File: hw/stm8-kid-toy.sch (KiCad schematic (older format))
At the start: 13 parts, among them SW1 SW_Push, SW2 SW_Push, SW3 SW_Push, U1 STM8S003F3P

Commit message: hw: change multiplexing
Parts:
- removed D4, D5, D6: DIODE, symbol Simulation_SPICE:DIODE
- removed R1, R2, R3: R, symbol Device:R
- added D?: DIODE, symbol Simulation_SPICE:DIODE
- added R? (x6): R, symbol Device:R
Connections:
- net BTN1: now also SW1.2, R?.1
- net BTN2: now also SW2.2, R?.1
- net BTN3: now also SW3.2, R?.1
- net COM1: now also D1.2 (A), D2.2 (A), D3.2 (A), D?.1 (A); no longer SW1.1, SW2.1, SW3.1
- net GND: now also R?.2, R?.2, R?.2
- net LED1: now also R?.1; no longer D1.1 (K)
- net LED2: now also R?.1; no longer D2.1 (K)
- net LED3: now also R?.1; no longer D3.1 (K)
- new net: D1.1 (K), R?.2
- new net: D2.1 (K), R?.2
- new net: D3.1 (K), R?.2
- new net: D?.2 (K), SW1.1, SW2.1, SW3.1
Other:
- moved on the sheet: D1, D2, D3
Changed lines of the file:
@@
 	3000 1400 3000 1500
 Connection ~ 2500 1400
-Wire Wire Line
-	2000 1800 2000 1950
-Wire Wire Line
-	2500 1800 2500 1950
-Wire Wire Line
-	3000 1800 3000 1950
 Text GLabel 1750 1400 0    50   Input ~ 0
 COM1
-Text GLabel 1750 2650 0    50   Input ~ 0
+Text GLabel 1250 2550 0    50   Input ~ 0
 LED2
-Text GLabel 1750 2800 0    50   Input ~ 0
+Text GLabel 1250 2800 0    50   Input ~ 0
 LED3
 Wire Wire Line
-	1750 2500 2000 2500
-Wire Wire Line
-	2000 2500 2000 2250
-Wire Wire Line
-	2500 2250 2500 2650
-Wire Wire Line
-	2500 2650 1750 2650
-Wire Wire Line
-	1750 2800 3000 2800
-Wire Wire Line
-	3000 2800 3000 2250
+	2000 2325 2000 1800
+Wire Wire Line
+	2500 1800 2500 2550
+Wire Wire Line
+	3000 2800 3000 1800
 Wire Wire Line
 	3525 1400 3525 1500
@@
 	4625 1400 4625 1500
 Connection ~ 4075 1400
-Wire Wire Line
-	3525 1900 3525 2000
-Wire Wire Line
-	4075 1900 4075 2000
-Wire Wire Line
-	4625 1900 4625 2000
-Wire Wire Line
-	3525 2300 3525 2500
-Wire Wire Line
-	4075 2300 4075 2650
-$Comp
-L Device:R R1
-U 1 1 5D99B250
+$Comp
+L Device:LED D1
+U 1 1 5D99BF05
 P 2000 1650
-F 0 "R1" H 2070 1696 50  0000 L CNN
-F 1 "R" H 2070 1605 50  0000 L CNN
-F 2 "" V 1930 1650 50  0001 C CNN
+F 0 "D1" V 2039 1533 50  0000 R CNN
+F 1 "LED" V 1948 1533 50  0000 R CNN
+F 2 "" H 2000 1650 50  0001 C CNN
 F 3 "~" H 2000 1650 50  0001 C CNN
 	1    2000 1650
-	1    0    0    -1
-$EndComp
-$Comp
-L Device:R R2
-U 1 1 5D99B5EC
+	0    -1   -1   0
+$EndComp
+$Comp
+L Device:LED D2
+U 1 1 5D99C497
 P 2500 1650
-F 0 "R2" H 2570 1696 50  0000 L CNN
-F 1 "R" H 2570 1605 50  0000 L CNN
-F 2 "" V 2430 1650 50  0001 C CNN
+F 0 "D2" V 2539 1533 50  0000 R CNN
+F 1 "LED" V 2448 1533 50  0000 R CNN
+F 2 "" H 2500 1650 50  0001 C CNN
 F 3 "~" H 2500 1650 50  0001 C CNN
 	1    2500 1650
-	1    0    0    -1
-$EndComp
-$Comp
-L Device:R R3
-U 1 1 5D99B951
+	0    -1   -1   0
+$EndComp
+$Comp
+L Device:LED D3
+U 1 1 5D99C795
 P 3000 1650
-F 0 "R3" H 3070 1696 50  0000 L CNN
-F 1 "R" H 3070 1605 50  0000 L CNN
-F 2 "" V 2930 1650 50  0001 C CNN
+F 0 "D3" V 3039 1533 50  0000 R CNN
+F 1 "LED" V 2948 1533 50  0000 R CNN
+F 2 "" H 3000 1650 50  0001 C CNN
 F 3 "~" H 3000 1650 50  0001 C CNN
 	1    3000 1650
-	1    0    0    -1
-$EndComp
-$Comp
-L Device:LED D1
-U 1 1 5D99BF05
-P 2000 2100
-F 0 "D1" V 2039 1983 50  0000 R CNN
-F 1 "LED" V 1948 1983 50  0000 R CNN
-F 2 "" H 2000 2100 50  0001 C CNN
-F 3 "~" H 2000 2100 50  0001 C CNN
-	1    2000 2100
-	0    -1   -1   0
-$EndComp
-$Comp
-L Device:LED D2
-U 1 1 5D99C497
-P 2500 2100
-F 0 "D2" V 2539 1983 50  0000 R CNN
-F 1 "LED" V 2448 1983 50  0000 R CNN
-F 2 "" H 2500 2100 50  0001 C CNN
-F 3 "~" H 2500 2100 50  0001 C CNN
-	1    2500 2100
-	0    -1   -1   0
-$EndComp
-$Comp
-L Device:LED D3
-U 1 1 5D99C795
-P 3000 2100
-F 0 "D3" V 3039 1983 50  0000 R CNN
-F 1 "LED" V 2948 1983 50  0000 R CNN
-F 2 "" H 3000 2100 50  0001 C CNN
-F 3 "~" H 3000 2100 50  0001 C CNN
-	1    3000 2100
 	0    -1   -1   0
 $EndComp
@@
 F 3 "~" H 4625 1900 50  0001 C CNN
 	1    4625 1700
-	0    1    1    0
-$EndComp
-$Comp
-L Simulation_SPICE:DIODE D4
-U 1 1 5D99F3A7
-P 3525 2150
-F 0 "D4" V 3479 2230 50  0000 L CNN
-F 1 "DIODE" V 3570 2230 50  0000 L CNN
-F 2 "" H 3525 2150 50  0001 C CNN
-F 3 "~" H 3525 2150 50  0001 C CNN
-F 4 "Y" H 3525 2150 50  0001 L CNN "Spice_Netlist_Enabled"
-F 5 "V" H 3525 2150 50  0001 L CNN "Spice_Primitive"
-	1    3525 2150
-	0    1    1    0
-$EndComp
-$Comp
-L Simulation_SPICE:DIODE D5
-U 1 1 5D99FC49
-P 4075 2150
-F 0 "D5" V 4029 2230 50  0000 L CNN
-F 1 "DIODE" V 4120 2230 50  0000 L CNN
-F 2 "" H 4075 2150 50  0001 C CNN
-F 3 "~" H 4075 2150 50  0001 C CNN
-F 4 "Y" H 4075 2150 50  0001 L CNN "Spice_Netlist_Enabled"
-F 5 "V" H 4075 2150 50  0001 L CNN "Spice_Primitive"
-	1    4075 2150
-	0    1    1    0
-$EndComp
-$Comp
-L Simulation_SPICE:DIODE D6
-U 1 1 5D99FF83
-P 4625 2150
-F 0 "D6" V 4579 2230 50  0000 L CNN
-F 1 "DIODE" V 4670 2230 50  0000 L CNN
-F 2 "" H 4625 2150 50  0001 C CNN
-F 3 "~" H 4625 2150 50  0001 C CNN
-F 4 "Y" H 4625 2150 50  0001 L CNN "Spice_Netlist_Enabled"
-F 5 "V" H 4625 2150 50  0001 L CNN "Spice_Primitive"
-	1    4625 2150
 	0    1    1    0
 $EndComp
@@
 Wire Wire Line
 	4200 5650 4400 5650
-Connection ~ 3000 1400
-Connection ~ 3525 1400
 Wire Wire Line
 	1750 1400 2000 1400
 Connection ~ 2000 1400
-Text GLabel 1750 2500 0    50   Input ~ 0
+Text GLabel 1250 2325 0    50   Input ~ 0
 LED1
-Wire Wire Line
-	3000 1400 3525 1400
 Wire Wire Line
 	2500 1400 3000 1400
@@
 Wire Wire Line
 	3400 2800 4625 2800
-Wire Wire Line
-	4625 2800 4625 2300
+$Comp
+L Simulation_SPICE:DIODE D?
+U 1 1 5DA61785
+P 3250 1400
+F 0 "D?" V 3204 1480 50  0000 L CNN
+F 1 "DIODE" V 3295 1480 50  0000 L CNN
+F 2 "" H 3250 1400 50  0001 C CNN
+F 3 "~" H 3250 1400 50  0001 C CNN
+F 4 "Y" H 3250 1400 50  0001 L CNN "Spice_Netlist_Enabled"
+F 5 "V" H 3250 1400 50  0001 L CNN "Spice_Primitive"
+	1    3250 1400
+	1    0    0    -1
+$EndComp
+Wire Wire Line
+	3000 1400 3100 1400
+Connection ~ 3000 1400
+Wire Wire Line
+	3400 1400 3525 1400
+Connection ~ 3525 1400
+Wire Wire Line
+	3525 1900 3525 2200
+Wire Wire Line
+	4075 1900 4075 2400
+Wire Wire Line
+	4625 1900 4625 2675
+$Comp
+L Device:R R?
+U 1 1 5DA674E2
+P 1500 2325
+F 0 "R?" H 1570 2371 50  0000 L CNN
+F 1 "R" H 1570 2280 50  0000 L CNN
+F 2 "" V 1430 2325 50  0001 C CNN
+F 3 "~" H 1500 2325 50  0001 C CNN
+	1    1500 2325
+	0    -1   -1   0
+$EndComp
+$Comp
+L Device:R R?
+U 1 1 5DA68A52
+P 1500 2550
+F 0 "R?" H 1570 2596 50  0000 L CNN
+F 1 "R" H 1570 2505 50  0000 L CNN
+F 2 "" V 1430 2550 50  0001 C CNN
+F 3 "~" H 1500 2550 50  0001 C CNN
+	1    1500 2550
+	0    -1   -1   0
+$EndComp
+$Comp
+L Device:R R?
+U 1 1 5DA68F22
+P 1500 2800
+F 0 "R?" H 1570 2846 50  0000 L CNN
+F 1 "R" H 1570 2755 50  0000 L CNN
+F 2 "" V 1430 2800 50  0001 C CNN
+F 3 "~" H 1500 2800 50  0001 C CNN
+	1    1500 2800
+	0    -1   -1   0
+$EndComp
+Wire Wire Line
+	3000 2800 1650 2800
+Wire Wire Line
+	1650 2550 2500 2550
+Wire Wire Line
+	2000 2325 1650 2325
+Wire Wire Line
+	1250 2325 1350 2325
+Wire Wire Line
+	1350 2550 1250 2550
+Wire Wire Line
+	1250 2800 1350 2800
+$Comp
+L Device:R R?
+U 1 1 5DA73BCF
+P 3750 2200
+F 0 "R?" H 3820 2246 50  0000 L CNN
+F 1 "R" H 3820 2155 50  0000 L CNN
+F 2 "" V 3680 2200 50  0001 C CNN
+F 3 "~" H 3750 2200 50  0001 C CNN
+	1    3750 2200
+	0    -1   -1   0
+$EndComp
+$Comp
+L Device:R R?
+U 1 1 5DA74885
+P 4275 2400
+F 0 "R?" H 4345 2446 50  0000 L CNN
+F 1 "R" H 4345 2355 50  0000 L CNN
+F 2 "" V 4205 2400 50  0001 C CNN
+F 3 "~" H 4275 2400 50  0001 C CNN
+	1    4275 2400
+	0    -1   -1   0
+$EndComp
+$Comp
+L Device:R R?
+U 1 1 5DA74D1A
+P 4850 2675
+F 0 "R?" H 4920 2721 50  0000 L CNN
+F 1 "R" H 4920 2630 50  0000 L CNN
+F 2 "" V 4780 2675 50  0001 C CNN
+F 3 "~" H 4850 2675 50  0001 C CNN
+	1    4850 2675
+	0    -1   -1   0
+$EndComp
+Wire Wire Line
+	3525 2200 3600 2200
+Connection ~ 3525 2200
+Wire Wire Line
+	3525 2200 3525 2500
+Wire Wire Line
+	4125 2400 4075 2400
+Connection ~ 4075 2400
+Wire Wire Line
+	4075 2400 4075 2650
+Wire Wire Line
+	4700 2675 4625 2675
+Connection ~ 4625 2675
+Wire Wire Line
+	4625 2675 4625 2800
+Wire Wire Line
+	5000 2675 5150 2675
+Wire Wire Line
+	4425 2400 5150 2400
+Wire Wire Line
+	5150 2400 5150 2675
+Wire Wire Line
+	3900 2200 5150 2200
+Wire Wire Line
+	5150 2200 5150 2400
+Connection ~ 5150 2400
+Text GLabel 5250 2675 2    50   Input ~ 0
+GND
+Wire Wire Line
+	5250 2675 5150 2675
+Connection ~ 5150 2675
 $EndSCHEMATC

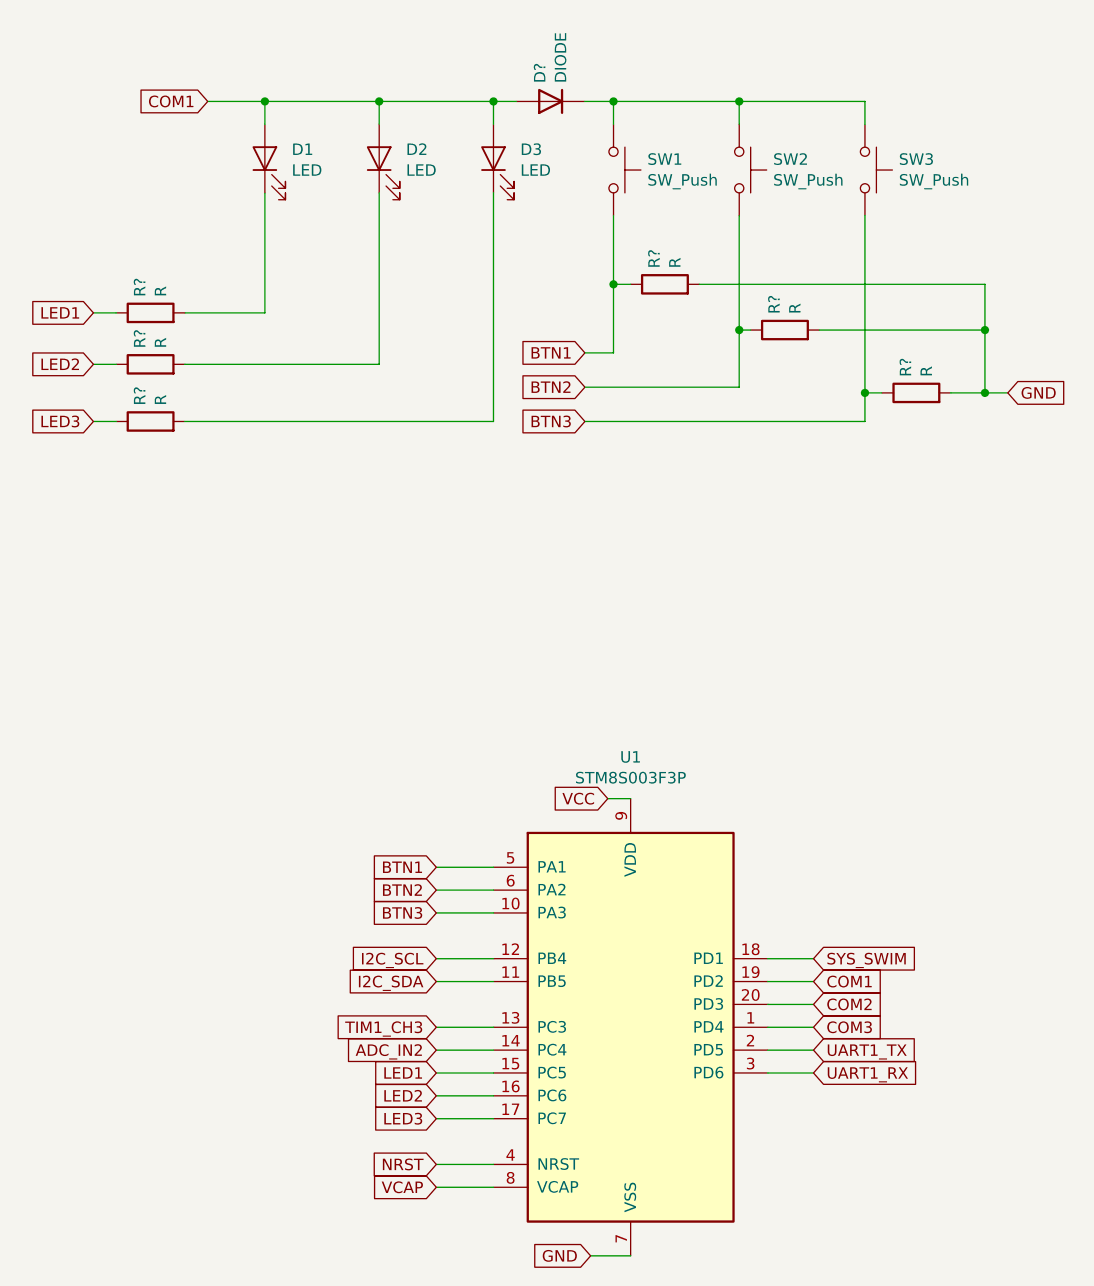
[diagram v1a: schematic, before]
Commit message: update sch: gpio and btn mux
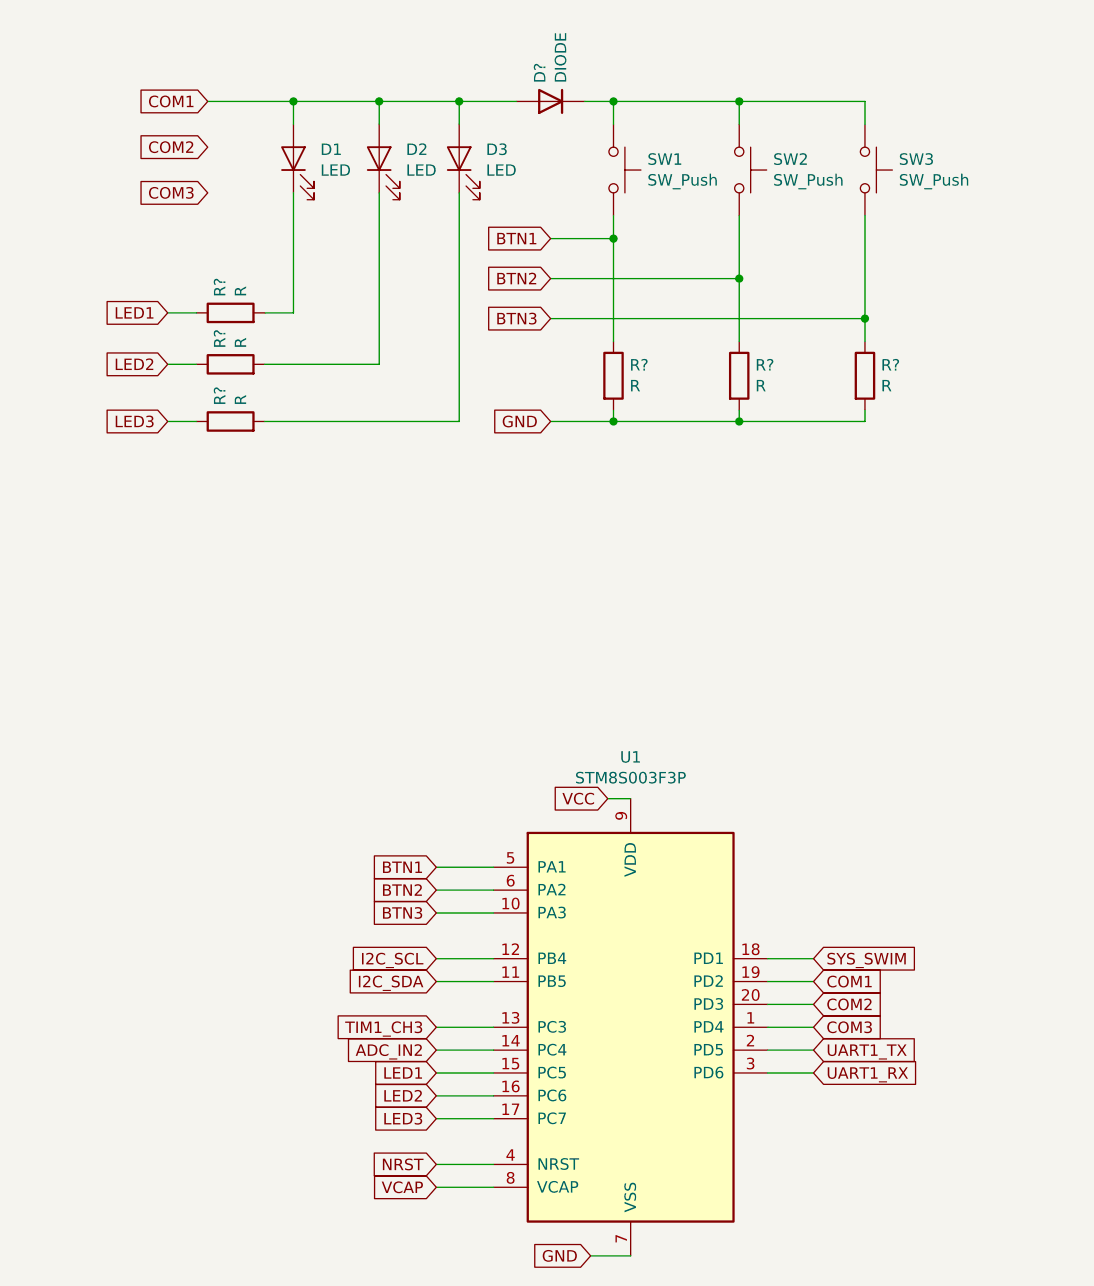
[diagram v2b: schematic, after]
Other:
- moved on the sheet: D1, D3, R?
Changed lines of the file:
@@
 $EndDescr
 Wire Wire Line
-	2000 1400 2500 1400
+	2125 1400 2500 1400
 Wire Wire Line
 	2500 1400 2500 1500
 Wire Wire Line
-	2000 1400 2000 1500
-Wire Wire Line
-	3000 1400 3000 1500
+	2125 1400 2125 1500
+Wire Wire Line
+	2850 1400 2850 1500
 Connection ~ 2500 1400
 Text GLabel 1750 1400 0    50   Input ~ 0
 COM1
-Text GLabel 1250 2550 0    50   Input ~ 0
+Text GLabel 1575 2550 0    50   Input ~ 0
 LED2
-Text GLabel 1250 2800 0    50   Input ~ 0
+Text GLabel 1575 2800 0    50   Input ~ 0
 LED3
 Wire Wire Line
-	2000 2325 2000 1800
+	2125 2325 2125 1800
 Wire Wire Line
 	2500 1800 2500 2550
 Wire Wire Line
-	3000 2800 3000 1800
+	2850 2800 2850 1800
 Wire Wire Line
 	3525 1400 3525 1500
@@
 L Device:LED D1
 U 1 1 5D99BF05
-P 2000 1650
-F 0 "D1" V 2039 1533 50  0000 R CNN
-F 1 "LED" V 1948 1533 50  0000 R CNN
-F 2 "" H 2000 1650 50  0001 C CNN
-F 3 "~" H 2000 1650 50  0001 C CNN
-	1    2000 1650
+P 2125 1650
+F 0 "D1" V 2164 1533 50  0000 R CNN
+F 1 "LED" V 2073 1533 50  0000 R CNN
+F 2 "" H 2125 1650 50  0001 C CNN
+F 3 "~" H 2125 1650 50  0001 C CNN
+	1    2125 1650
 	0    -1   -1   0
 $EndComp
@@
 L Device:LED D3
 U 1 1 5D99C795
-P 3000 1650
-F 0 "D3" V 3039 1533 50  0000 R CNN
-F 1 "LED" V 2948 1533 50  0000 R CNN
-F 2 "" H 3000 1650 50  0001 C CNN
-F 3 "~" H 3000 1650 50  0001 C CNN
-	1    3000 1650
+P 2850 1650
+F 0 "D3" V 2889 1533 50  0000 R CNN
+F 1 "LED" V 2798 1533 50  0000 R CNN
+F 2 "" H 2850 1650 50  0001 C CNN
+F 3 "~" H 2850 1650 50  0001 C CNN
+	1    2850 1650
 	0    -1   -1   0
 $EndComp
@@
 	4200 5650 4400 5650
 Wire Wire Line
-	1750 1400 2000 1400
-Connection ~ 2000 1400
-Text GLabel 1250 2325 0    50   Input ~ 0
+	1750 1400 2125 1400
+Connection ~ 2125 1400
+Text GLabel 1575 2325 0    50   Input ~ 0
 LED1
 Wire Wire Line
-	2500 1400 3000 1400
-Text GLabel 3400 2500 0    50   Input ~ 0
+	2500 1400 2850 1400
+Text GLabel 3250 2000 0    50   Input ~ 0
 BTN1
-Text GLabel 3400 2650 0    50   Input ~ 0
+Text GLabel 3250 2175 0    50   Input ~ 0
 BTN2
-Text GLabel 3400 2800 0    50   Input ~ 0
+Text GLabel 3250 2350 0    50   Input ~ 0
 BTN3
 Wire Wire Line
-	3400 2500 3525 2500
-Wire Wire Line
-	3400 2650 4075 2650
-Wire Wire Line
-	3400 2800 4625 2800
+	3250 2000 3525 2000
+Wire Wire Line
+	3250 2175 4075 2175
+Wire Wire Line
+	3250 2350 4625 2350
 $Comp
 L Simulation_SPICE:DIODE D?
@@
 $EndComp
 Wire Wire Line
-	3000 1400 3100 1400
-Connection ~ 3000 1400
+	2850 1400 3100 1400
+Connection ~ 2850 1400
 Wire Wire Line
 	3400 1400 3525 1400
 Connection ~ 3525 1400
-Wire Wire Line
-	3525 1900 3525 2200
-Wire Wire Line
-	4075 1900 4075 2400
-Wire Wire Line
-	4625 1900 4625 2675
 $Comp
 L Device:R R?
 U 1 1 5DA674E2
-P 1500 2325
-F 0 "R?" H 1570 2371 50  0000 L CNN
-F 1 "R" H 1570 2280 50  0000 L CNN
-F 2 "" V 1430 2325 50  0001 C CNN
-F 3 "~" H 1500 2325 50  0001 C CNN
-	1    1500 2325
+P 1850 2325
+F 0 "R?" H 1920 2371 50  0000 L CNN
+F 1 "R" H 1920 2280 50  0000 L CNN
+F 2 "" V 1780 2325 50  0001 C CNN
+F 3 "~" H 1850 2325 50  0001 C CNN
+	1    1850 2325
 	0    -1   -1   0
 $EndComp
@@
 L Device:R R?
 U 1 1 5DA68A52
-P 1500 2550
-F 0 "R?" H 1570 2596 50  0000 L CNN
-F 1 "R" H 1570 2505 50  0000 L CNN
-F 2 "" V 1430 2550 50  0001 C CNN
-F 3 "~" H 1500 2550 50  0001 C CNN
-	1    1500 2550
+P 1850 2550
+F 0 "R?" H 1920 2596 50  0000 L CNN
+F 1 "R" H 1920 2505 50  0000 L CNN
+F 2 "" V 1780 2550 50  0001 C CNN
+F 3 "~" H 1850 2550 50  0001 C CNN
+	1    1850 2550
 	0    -1   -1   0
 $EndComp
@@
 L Device:R R?
 U 1 1 5DA68F22
-P 1500 2800
-F 0 "R?" H 1570 2846 50  0000 L CNN
-F 1 "R" H 1570 2755 50  0000 L CNN
-F 2 "" V 1430 2800 50  0001 C CNN
-F 3 "~" H 1500 2800 50  0001 C CNN
-	1    1500 2800
-	0    -1   -1   0
-$EndComp
-Wire Wire Line
-	3000 2800 1650 2800
-Wire Wire Line
-	1650 2550 2500 2550
-Wire Wire Line
-	2000 2325 1650 2325
-Wire Wire Line
-	1250 2325 1350 2325
-Wire Wire Line
-	1350 2550 1250 2550
-Wire Wire Line
-	1250 2800 1350 2800
+P 1850 2800
+F 0 "R?" H 1920 2846 50  0000 L CNN
+F 1 "R" H 1920 2755 50  0000 L CNN
+F 2 "" V 1780 2800 50  0001 C CNN
+F 3 "~" H 1850 2800 50  0001 C CNN
+	1    1850 2800
+	0    -1   -1   0
+$EndComp
+Wire Wire Line
+	2850 2800 2000 2800
+Wire Wire Line
+	2000 2550 2500 2550
+Wire Wire Line
+	2125 2325 2000 2325
+Wire Wire Line
+	1575 2325 1700 2325
+Wire Wire Line
+	1700 2550 1575 2550
+Wire Wire Line
+	1575 2800 1700 2800
+$Comp
+L Device:R R?
+U 1 1 5DA74885
+P 4075 2600
+F 0 "R?" H 4145 2646 50  0000 L CNN
+F 1 "R" H 4145 2555 50  0000 L CNN
+F 2 "" V 4005 2600 50  0001 C CNN
+F 3 "~" H 4075 2600 50  0001 C CNN
+	1    4075 2600
+	1    0    0    -1
+$EndComp
+$Comp
+L Device:R R?
+U 1 1 5DA74D1A
+P 4625 2600
+F 0 "R?" H 4695 2646 50  0000 L CNN
+F 1 "R" H 4695 2555 50  0000 L CNN
+F 2 "" V 4555 2600 50  0001 C CNN
+F 3 "~" H 4625 2600 50  0001 C CNN
+	1    4625 2600
+	1    0    0    -1
+$EndComp
+Text GLabel 3250 2800 0    50   Input ~ 0
+GND
 $Comp
 L Device:R R?
 U 1 1 5DA73BCF
-P 3750 2200
-F 0 "R?" H 3820 2246 50  0000 L CNN
-F 1 "R" H 3820 2155 50  0000 L CNN
-F 2 "" V 3680 2200 50  0001 C CNN
-F 3 "~" H 3750 2200 50  0001 C CNN
-	1    3750 2200
-	0    -1   -1   0
-$EndComp
-$Comp
-L Device:R R?
-U 1 1 5DA74885
-P 4275 2400
-F 0 "R?" H 4345 2446 50  0000 L CNN
-F 1 "R" H 4345 2355 50  0000 L CNN
-F 2 "" V 4205 2400 50  0001 C CNN
-F 3 "~" H 4275 2400 50  0001 C CNN
-	1    4275 2400
-	0    -1   -1   0
-$EndComp
-$Comp
-L Device:R R?
-U 1 1 5DA74D1A
-P 4850 2675
-F 0 "R?" H 4920 2721 50  0000 L CNN
-F 1 "R" H 4920 2630 50  0000 L CNN
-F 2 "" V 4780 2675 50  0001 C CNN
-F 3 "~" H 4850 2675 50  0001 C CNN
-	1    4850 2675
-	0    -1   -1   0
-$EndComp
-Wire Wire Line
-	3525 2200 3600 2200
-Connection ~ 3525 2200
-Wire Wire Line
-	3525 2200 3525 2500
-Wire Wire Line
-	4125 2400 4075 2400
-Connection ~ 4075 2400
-Wire Wire Line
-	4075 2400 4075 2650
-Wire Wire Line
-	4700 2675 4625 2675
-Connection ~ 4625 2675
-Wire Wire Line
-	4625 2675 4625 2800
-Wire Wire Line
-	5000 2675 5150 2675
-Wire Wire Line
-	4425 2400 5150 2400
-Wire Wire Line
-	5150 2400 5150 2675
-Wire Wire Line
-	3900 2200 5150 2200
-Wire Wire Line
-	5150 2200 5150 2400
-Connection ~ 5150 2400
-Text GLabel 5250 2675 2    50   Input ~ 0
-GND
-Wire Wire Line
-	5250 2675 5150 2675
-Connection ~ 5150 2675
+P 3525 2600
+F 0 "R?" H 3595 2646 50  0000 L CNN
+F 1 "R" H 3595 2555 50  0000 L CNN
+F 2 "" V 3455 2600 50  0001 C CNN
+F 3 "~" H 3525 2600 50  0001 C CNN
+	1    3525 2600
+	1    0    0    -1
+$EndComp
+Wire Wire Line
+	3525 1900 3525 2000
+Wire Wire Line
+	4075 1900 4075 2175
+Wire Wire Line
+	4625 1900 4625 2350
+Wire Wire Line
+	3525 2000 3525 2450
+Connection ~ 3525 2000
+Wire Wire Line
+	4075 2175 4075 2450
+Connection ~ 4075 2175
+Wire Wire Line
+	4625 2350 4625 2450
+Connection ~ 4625 2350
+Wire Wire Line
+	4625 2750 4625 2800
+Wire Wire Line
+	4625 2800 4075 2800
+Wire Wire Line
+	3525 2750 3525 2800
+Connection ~ 3525 2800
+Wire Wire Line
+	3525 2800 3250 2800
+Wire Wire Line
+	4075 2750 4075 2800
+Connection ~ 4075 2800
+Wire Wire Line
+	4075 2800 3525 2800
+Text GLabel 1750 1600 0    50   Input ~ 0
+COM2
+Text GLabel 1750 1800 0    50   Input ~ 0
+COM3
 $EndSCHEMATC
